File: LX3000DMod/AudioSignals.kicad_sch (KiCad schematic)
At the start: 13 parts

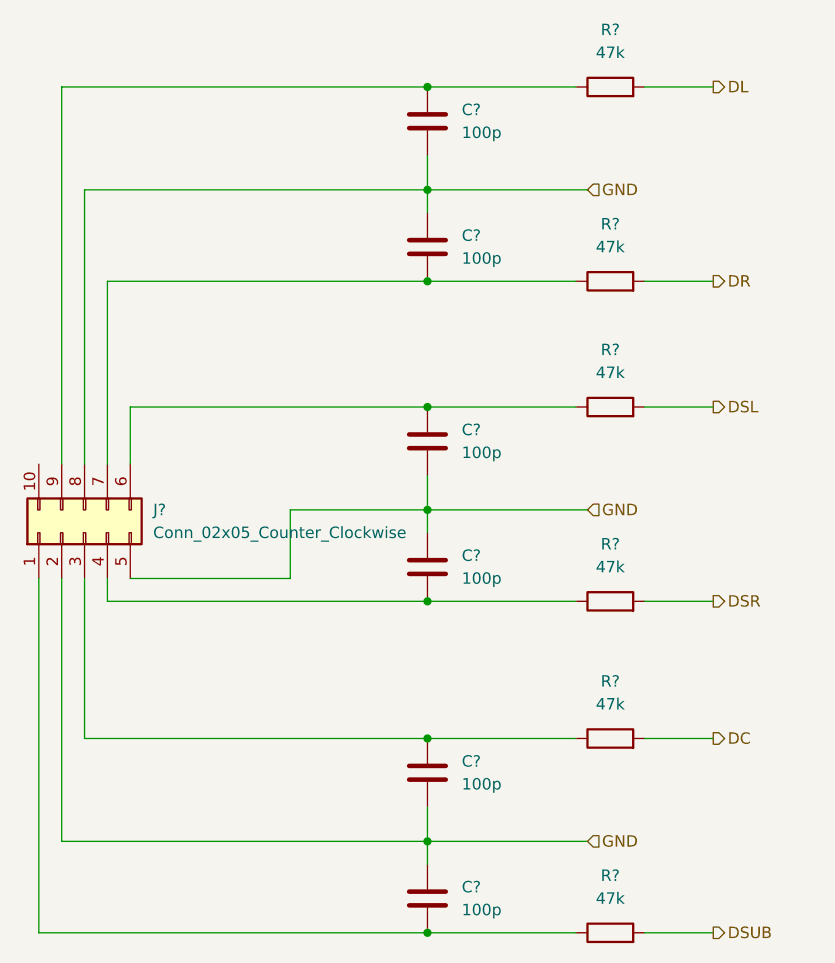
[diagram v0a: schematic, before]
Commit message: 10.8 PSU done
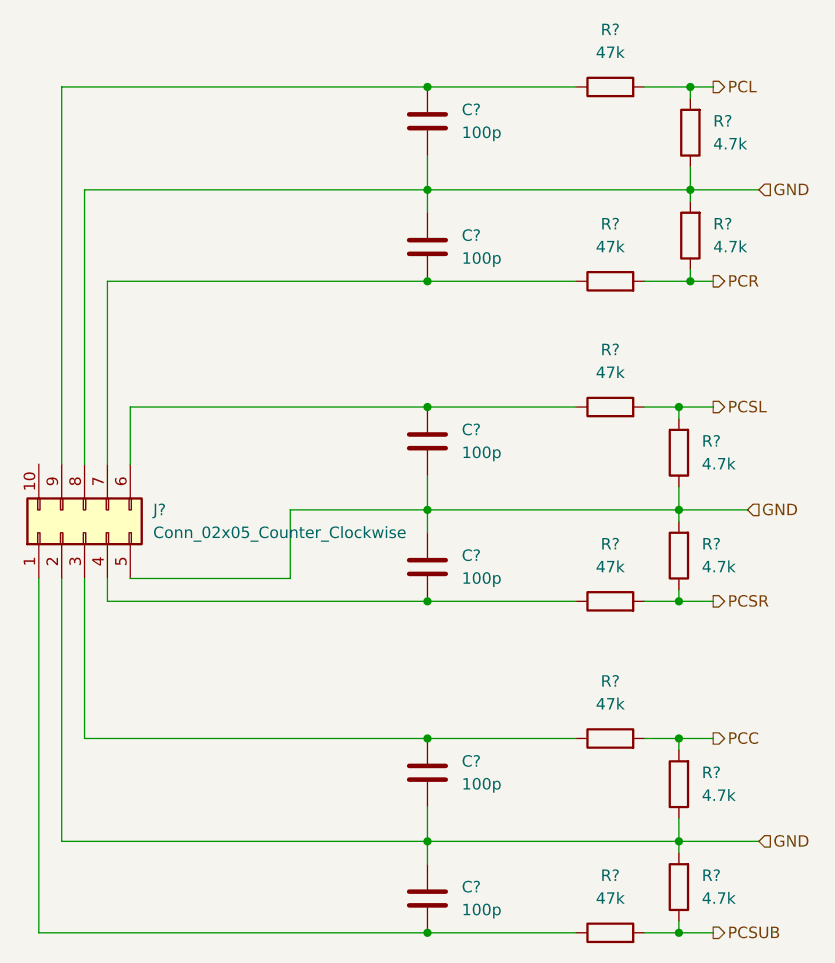
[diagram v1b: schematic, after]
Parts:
- added R? (x6): 4.7k, symbol Device:R
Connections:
- net GND: now also R?.1, R?.1, R?.1, R?.2, R?.2, R?.2
- net DC renamed PCC
- net PCC: now also R?.2
- net DL renamed PCL
- net PCL: now also R?.2
- net DR renamed PCR
- net PCR: now also R?.1
- net DSL renamed PCSL
- net PCSL: now also R?.2
- net DSR renamed PCSR
- net PCSR: now also R?.1
- net DSUB renamed PCSUB
- net PCSUB: now also R?.1

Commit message: updated repo and bkp state
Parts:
- C10, C11, C12, C13, C14, C9: renamed from C?; Spice_Model 100p -> (none); Spice_Netlist_Enabled Y -> (none); Spice_Primitive C -> (none)
- R13, R14, R15, R16, R17, R18: renamed from R?; Spice_Model 47k -> (none); Spice_Netlist_Enabled Y -> (none); Spice_Primitive R -> (none)
- R19, R20, R21, R22, R23, R24: renamed from R?; Spice_Model 4.7k -> (none); Spice_Netlist_Enabled Y -> (none); Spice_Primitive R -> (none)
- gave numbers to parts that had none: 1
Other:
- title: AudioSignals -> AudioSignalsInput
